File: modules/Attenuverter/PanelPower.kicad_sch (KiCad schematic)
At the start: 26 parts, among them J1 WQP-PJ398, J10 Conn_Front, J11 Conn_Back, J2 WQP-PJ398, J3 WQP-PJ398, J4 WQP-PJ398, J9 Conn_Eurorack_Pwr_10, U1 TL074, U2 TL074, U3 LM4040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

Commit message: Attenuverter - wip
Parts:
- D2: Label LED-1 -> LED-2
- RV3: Label GAIN-1 -> GAIN-2
- RV4: Label OFFSET-1 -> OFFSET-2

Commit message: Attenuverter - wip
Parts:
- added J7: Conn_Front, Connector_PinSocket_2.54mm:PinSocket_1x09_P2.54mm_Vertical, symbol Connector_Generic:Conn_01x09
- added J8: Conn_Back, Connector_PinHeader_2.54mm:PinHeader_1x09_P2.54mm_Horizontal, symbol Connector_Generic:Conn_01x09
- J5: renamed from J10; footprint Connector_PinSocket_2.54mm:PinSocket_1x18_P2.54mm_Vertical -> Connector_PinSocket_2.54mm:PinSocket_1x09_P2.54mm_Vertical; symbol Connector_Generic:Conn_01x18 -> Connector_Generic:Conn_01x09
- J6: renamed from J11; footprint Connector_PinHeader_2.54mm:PinHeader_1x18_P2.54mm_Horizontal -> Connector_PinHeader_2.54mm:PinHeader_1x09_P2.54mm_Horizontal; symbol Connector_Generic:Conn_01x18 -> Connector_Generic:Conn_01x09
- U3, U4: footprint -lmp-misc:TO-92-2_Wide -> -lmp-misc:TO-92-2_Inline
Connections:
- net +5VREF: now also J7.1 (Pin_1), J8.1 (Pin_1); no longer J5.16 (Pin_16), J6.16 (Pin_16)
- net -5VREF: now also J5.9 (Pin_9), J6.9 (Pin_9); no longer J5.17 (Pin_17), J6.17 (Pin_17)
- net GAIN-2: now also J7.2 (Pin_2), J8.2 (Pin_2); no longer J5.9 (Pin_9), J6.9 (Pin_9)
- net GAIN-POT-2: now also J7.3 (Pin_3), J8.3 (Pin_3); no longer J5.10 (Pin_10), J6.10 (Pin_10)
- net GND: now also J7.9 (Pin_9), J8.9 (Pin_9); no longer J5.18 (Pin_18), J6.18 (Pin_18)
- net IN-1: now also J5.8 (Pin_8), J6.8 (Pin_8); no longer J5.6 (Pin_6), J6.6 (Pin_6)
- net IN-2: now also J7.8 (Pin_8), J8.8 (Pin_8); no longer J5.14 (Pin_14), J6.14 (Pin_14)
- net LED-2-1: now also J7.5 (Pin_5), J8.5 (Pin_5); no longer J5.12 (Pin_12), J6.12 (Pin_12)
- net LED-2-2: now also J7.6 (Pin_6), J8.6 (Pin_6); no longer J5.13 (Pin_13), J6.13 (Pin_13)
- net OFFSET-2: now also J7.4 (Pin_4), J8.4 (Pin_4); no longer J5.11 (Pin_11), J6.11 (Pin_11)
- net OUT-1: now also J5.7 (Pin_7), J6.7 (Pin_7); no longer J5.8 (Pin_8), J6.8 (Pin_8)
- net OUT-1-NORMAL: now also J5.6 (Pin_6), J6.6 (Pin_6); no longer J5.7 (Pin_7), J6.7 (Pin_7)
- net OUT-2: now also J7.7 (Pin_7), J8.7 (Pin_7); no longer J5.15 (Pin_15), J6.15 (Pin_15)
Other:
- note added: "TODO: Split into two connectors to fit on PCB"

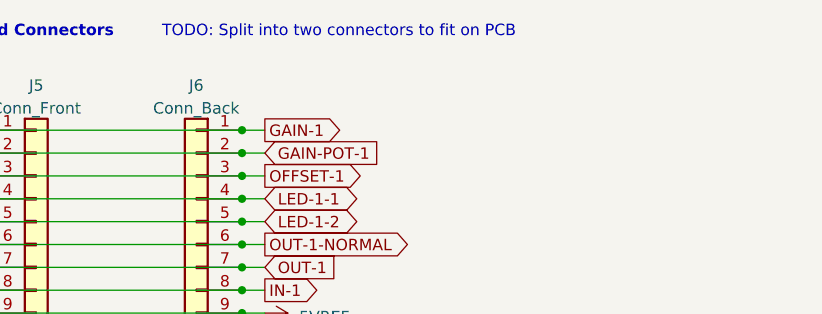
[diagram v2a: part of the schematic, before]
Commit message: Attenuverter - PCB layout finished
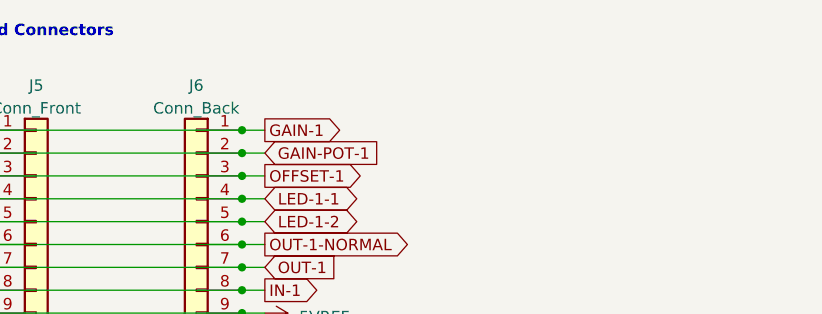
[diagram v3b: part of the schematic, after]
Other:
- note removed: "TODO: Split into two connectors to fit on PCB"

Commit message: Attenuverter - wip
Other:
- note added: "For best results, select gain potentiometers RV1 & RV2 as close to 100K as possible."

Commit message: Attenuverter - PCB tweaks
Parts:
- R1, R2: DistributorPartLink https://www.mouser.ca/c/?m=YAGEO&power+rating=166+mW+(1%2f6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 -> https://www.mouser.ca/ProductDetail/YAGEO/MFR-12FTF52-4K7?q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; DistributorPartNum 603-MFR-12* -> 603-MFR-12FTF52-4K7; ManufacturerPartNum MFR-12* -> MFR-12FTF52-4K7
- U3, U4: DistributorPartLink https://www.mouser.ca/c/semiconductors/integrated-circuits-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 -> https://www.mouser.ca/ProductDetail/Texas-Instruments/LM404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; DistributorPartNum (none) -> 926-LM4040BIZ50NOPB; ManufacturerPartNum LM4040* -> LM4040BIZ-5.0/NOPB

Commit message: Attenuverter - schematic correction
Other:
- note added: "For best results, select gain potentiometers RV1 & RV3 as close to 100K as possible."
- note removed: "For best results, select gain potentiometers RV1 & RV2 as close to 100K as possible."
